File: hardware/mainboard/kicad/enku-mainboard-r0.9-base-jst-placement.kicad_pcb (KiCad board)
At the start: 4 copper layers, 59 x 101 mm, 120 parts, among them J1 JST S3B-PH-SM4-TB(LF)(SN) 1S+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, J2 Hirose DM3AT-SF-PEJM5, J3 FH34SRJ-24S-0.5SH(50), J5 GCT USB4105-GF-A-120, J6 4-pin pogo dock, J7 Tag-Connect TC2030-IDC-NL, Q1 IRLML6346TRPBF, SW1 HARD POWER, SW2 BOOT / RECOVERY, SW3 BTN_L1, SW4 BTN_L2, SW5 BTN_R1, SW6 BTN_R2, U1 ESP32-S3-WROOM-1-N16R8, U2 TPS2121, U3 BQ25185DLHR, U4 TPS63802DLAR, U5 BMI270, U8 USBLC6-2SC6

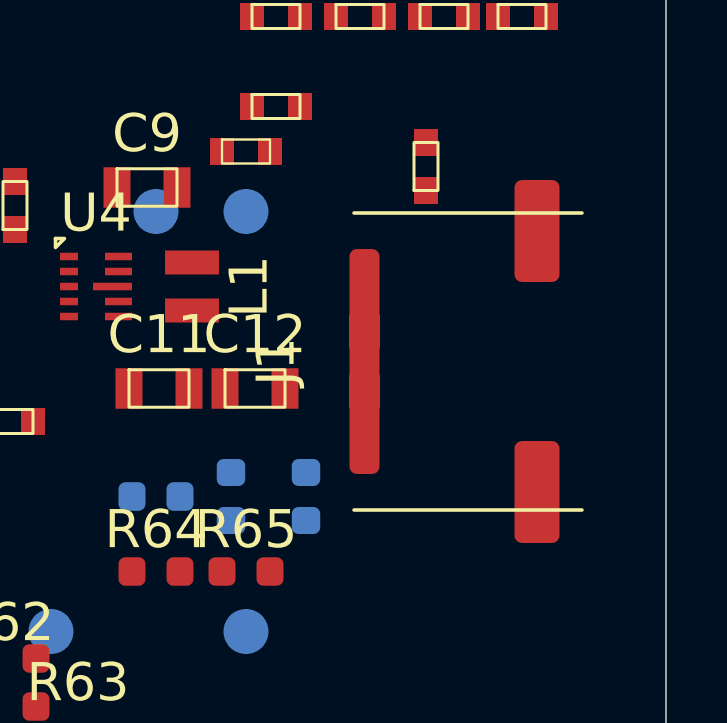
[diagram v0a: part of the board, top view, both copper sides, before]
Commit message: R32: fix rotated JST pad copper short + schematic parity; guard intra-footprint net clearance
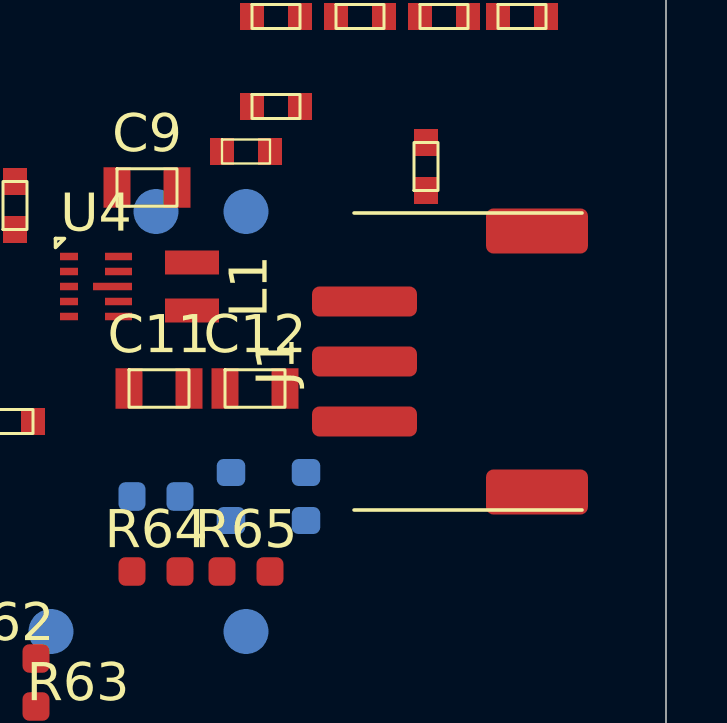
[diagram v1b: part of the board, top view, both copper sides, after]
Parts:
- J1: value JST S3B-PH-SM4-TB(LF)(SN) 1S+NTC -> 1S LiPo + NTC
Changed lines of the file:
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@@
     (at 69.8 93.5 90)
     (property "Reference" "J1" (at 0 -5.8 90) (layer "F.SilkS"))
-    (property "Value" "JST S3B-PH-SM4-TB(LF)(SN) 1S+NTC" (at 0 5.8 90) (layer "F.Fab") hide)
+    (property "Value" "1S LiPo + NTC" (at 0 5.8 90) (layer "F.Fab") hide)
     (attr smd)
     (fp_rect (start -5.6 -5.1) (end 5.6 5.1) (stroke (width 0.05) (type default)) (fill none) (layer "F.CrtYd"))
@@
     (fp_line (start 4.95 -3.2) (end 4.95 4.4) (stroke (width 0.12) (type default)) (layer "F.SilkS"))
     (fp_poly (pts (xy -2.5 -1.6) (xy -2 -0.892893) (xy -1.5 -1.6)) (stroke (width 0.1) (type default)) (fill none) (layer "F.Fab"))
-    (pad "MP" smd roundrect (at 4.35 2.9) (size 1.5 3.4) (layers "F.Cu" "F.Paste" "F.Mask") (roundrect_rratio 0.166667) (net 0 ""))
-    (pad "MP" smd roundrect (at -4.35 2.9) (size 1.5 3.4) (layers "F.Cu" "F.Paste" "F.Mask") (roundrect_rratio 0.166667) (net 0 ""))
-    (pad "1" smd roundrect (at -2 -2.85) (size 1 3.5) (layers "F.Cu" "F.Paste" "F.Mask") (roundrect_rratio 0.25) (net 80 "VBAT"))
-    (pad "2" smd roundrect (at 0 -2.85) (size 1 3.5) (layers "F.Cu" "F.Paste" "F.Mask") (roundrect_rratio 0.25) (net 1 "GND"))
-    (pad "3" smd roundrect (at 2 -2.85) (size 1 3.5) (layers "F.Cu" "F.Paste" "F.Mask") (roundrect_rratio 0.25) (net 91 "BAT_TS"))
+    (pad "MP" smd roundrect (at 4.35 2.9 90) (size 1.5 3.4) (layers "F.Cu" "F.Paste" "F.Mask") (roundrect_rratio 0.166667) (net 0 ""))
+    (pad "MP" smd roundrect (at -4.35 2.9 90) (size 1.5 3.4) (layers "F.Cu" "F.Paste" "F.Mask") (roundrect_rratio 0.166667) (net 0 ""))
+    (pad "1" smd roundrect (at -2 -2.85 90) (size 1 3.5) (layers "F.Cu" "F.Paste" "F.Mask") (roundrect_rratio 0.25) (net 80 "VBAT"))
+    (pad "2" smd roundrect (at 0 -2.85 90) (size 1 3.5) (layers "F.Cu" "F.Paste" "F.Mask") (roundrect_rratio 0.25) (net 1 "GND"))
+    (pad "3" smd roundrect (at 2 -2.85 90) (size 1 3.5) (layers "F.Cu" "F.Paste" "F.Mask") (roundrect_rratio 0.25) (net 91 "BAT_TS"))
   )
   (footprint "Capacitor_SMD:C_0805_2012Metric" (layer "F.Cu")
